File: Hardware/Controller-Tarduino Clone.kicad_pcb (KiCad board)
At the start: 2 copper layers, 34 x 34 mm, 25 parts, among them J1 Conn_01x07_Male, J2 Conn_01x04_Male, J3 Conn_01x02_Male, J4 Conn_01x02_Male, J5 Conn_01x02_Male, J6 Conn_01x02_Male, J7 Conn_01x08_Male, J9 QWIIC_Stackable, SW1 SW_Push, U1 ATmega328PB-A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

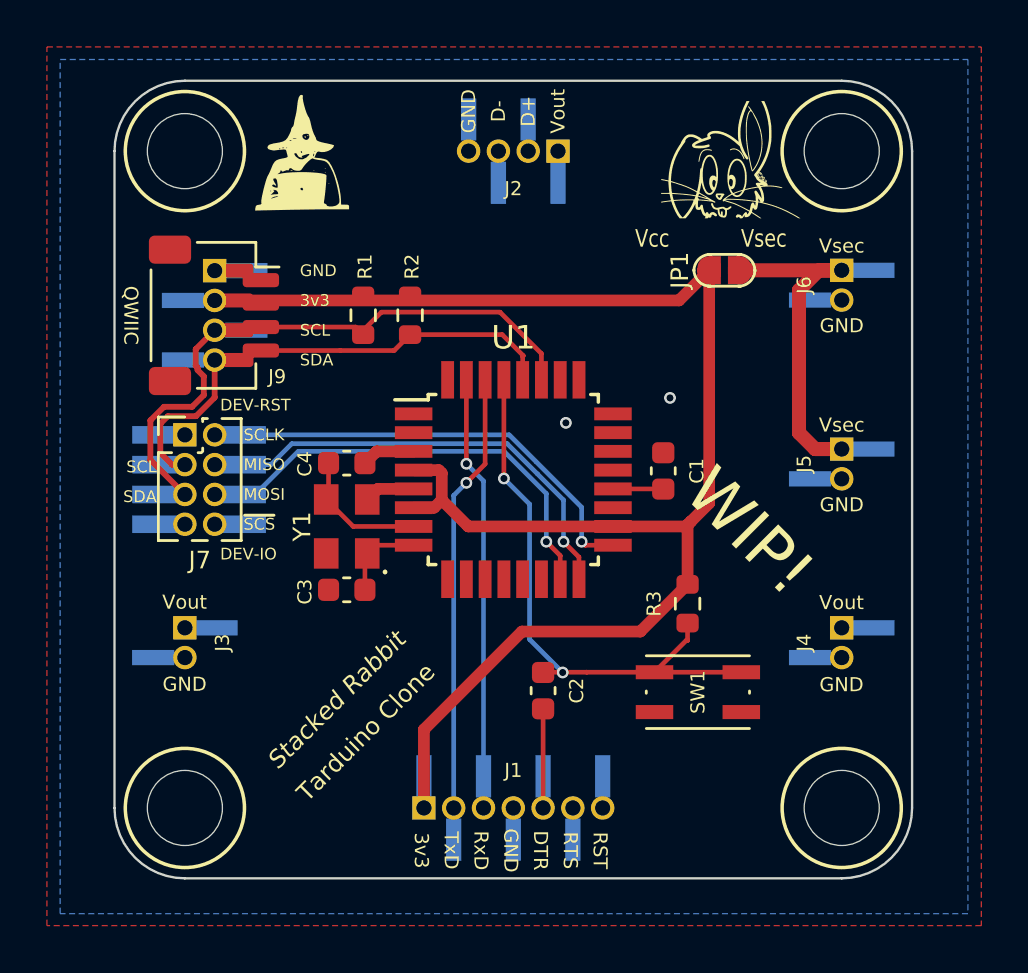
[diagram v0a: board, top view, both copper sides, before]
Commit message: Working on Controller-Tarduino Clone
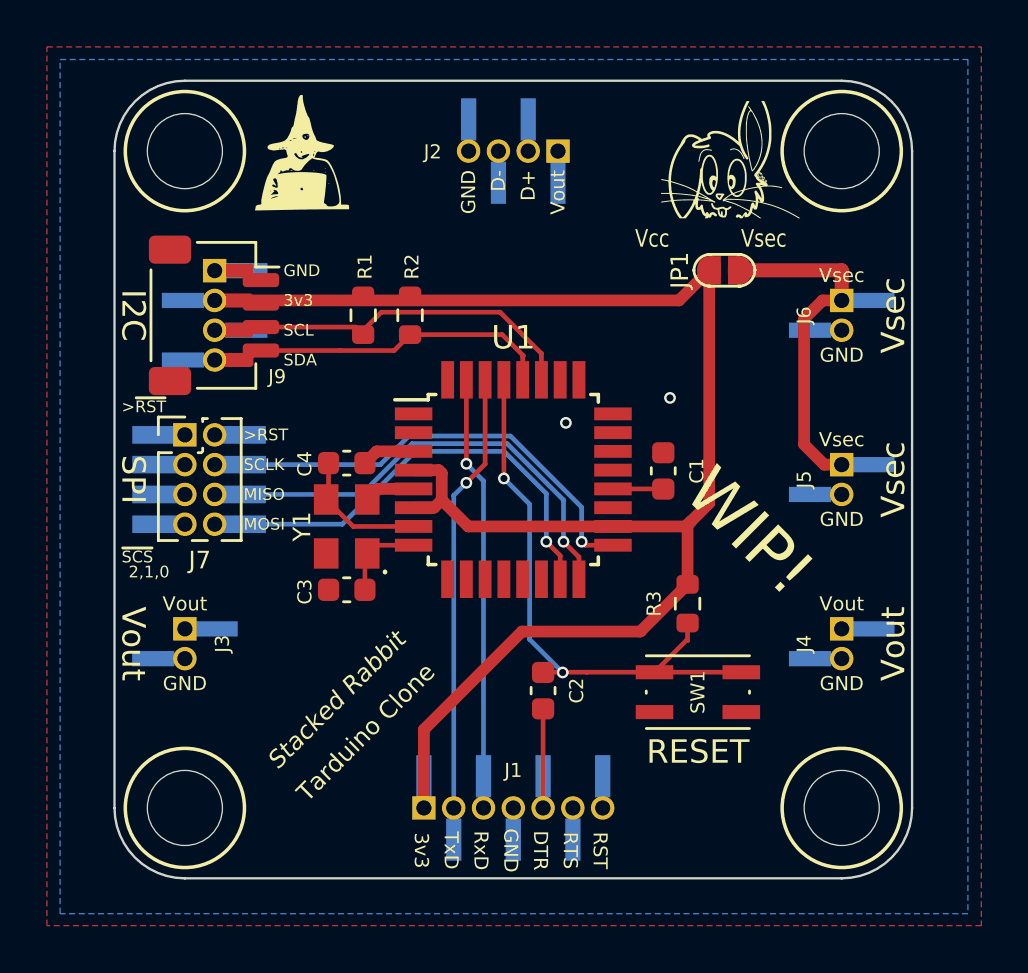
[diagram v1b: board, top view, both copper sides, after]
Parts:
- moved J6 1.28 mm to (114.0, 92.4)
- moved J5 0.66 mm to (114.0, 99.4)
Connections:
- net DEV_GPIO renamed ~{SCS}0
- net DEV_RST renamed ~{DEV_RESET}
- J7 pad 2: SCLK -> DEV_RESET
- J7 pad 3: SCL -> ~{SCS}2
- J7 pad 4: MISO -> SCLK
- J7 pad 5: SDA -> ~{SCS}1
- J7 pad 6: MOSI -> MISO
- J7 pad 8: ~{SCS} -> MOSI
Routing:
- net SDA: track 24.2 -> 14.4 mm
- net SCL: track 19.8 -> 12.9 mm
- net MISO: track 19.9 -> 20.4 mm
- net MOSI: track 19.5 -> 20.1 mm
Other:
- board text added: "2,1,0"
- board text added: ">RST"
- board text added: ">~{RST}"
- board text added: "I2C"
- board text added: "RESET"
- board text added: "SPI"
- board text removed: "DEV-IO"
- board text removed: "DEV-RST"
- board text removed: "QWIIC"

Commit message: Some tweaks
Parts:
- moved SW1 1.66 mm to (108.5, 110.6)
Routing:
- net RESET: track 24.7 -> 26.4 mm
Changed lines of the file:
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@@
   )
   (footprint "Tinker:SW_Push_TS273014TP" (layer "F.Cu")
-    (at 107.869419 109.062654 180)
+    (at 108.5 110.6 180)
     (descr "CK components KMR2 tactile switch http://www.ckswitches.com/media/1479/kmr2.pdf")
     (tags "tactile switch kmr2")
@@
     (effects (font (size 0.6 0.6) (thickness 0.125)))
   )
-  (gr_text "RESET" (at 107.869419 111.608369) (layer "F.SilkS")
+  (gr_text "RESET" (at 108.5 113) (layer "F.SilkS")
     (effects (font (size 1 1) (thickness 0.15)))
   )
@@
     (effects (font (size 1 1) (thickness 0.15)))
   )
-  (gr_text "${TITLE}" (at 93.718347 110.776452 45) (layer "F.SilkS")
+  (gr_text "${TITLE}" (at 93.267651 110.245027 45) (layer "F.SilkS")
     (effects (font (size 0.75 0.75) (thickness 0.15)))
   )
@@
   (segment (start 95.684592 98.471369) (end 99.74109 98.471369) (width 0.2) (layer "B.Cu") (net 26))
   (segment (start 99.74109 98.471369) (end 102.140751 100.87103) (width 0.2) (layer "B.Cu") (net 26))
-  (segment (start 106.019419 108.212654) (end 107.372873 106.8592) (width 0.2) (layer "F.Cu") (net 33))
-  (segment (start 106.019419 108.212654) (end 109.719419 108.212654) (width 0.2) (layer "F.Cu") (net 33))
-  (segment (start 107.372873 106.8592) (end 107.428728 106.8592) (width 0.2) (layer "F.Cu") (net 33))
-  (segment (start 107.428728 106.1173) (end 107.428728 106.8592) (width 0.2) (layer "F.Cu") (net 33))
+  (segment (start 106.65 109.75) (end 106.65 109.116441) (width 0.2) (layer "F.Cu") (net 33))
+  (segment (start 110.35 109.75) (end 106.65 109.75) (width 0.2) (layer "F.Cu") (net 33))
+  (segment (start 107.428728 106.1173) (end 107.428728 106.530139) (width 0.2) (layer "F.Cu") (net 33))
   (segment (start 99.6 99.954207) (end 99.6 95.75) (width 0.2) (layer "F.Cu") (net 33))
+  (segment (start 107.428728 106.530139) (end 105.746213 108.212654) (width 0.2) (layer "F.Cu") (net 33))
+  (segment (start 103.132654 108.212654) (end 105.746213 108.212654) (width 0.2) (layer "F.Cu") (net 33))
   (segment (start 101.27 108.225) (end 101.282346 108.212654) (width 0.2) (layer "F.Cu") (net 33))
+  (segment (start 106.65 109.116441) (end 105.746213 108.212654) (width 0.2) (layer "F.Cu") (net 33))
   (segment (start 101.282346 108.212654) (end 103.132654 108.212654) (width 0.2) (layer "F.Cu") (net 33))
-  (segment (start 103.132654 108.212654) (end 106.019419 108.212654) (width 0.2) (layer "F.Cu") (net 33))
   (via (at 99.6 99.954207) (size 0.5) (drill 0.3) (layers "F.Cu" "B.Cu") (net 33))
   (via (at 102.105196 108.224995) (size 0.5) (drill 0.3) (layers "F.Cu" "B.Cu") (net 33))
